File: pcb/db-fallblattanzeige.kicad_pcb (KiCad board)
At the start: 2 copper layers, 20 parts, among them IC1 ATMEGA328-P, IC2 MAX485, P1 2x9_pin_holes, P2 FTDI_header, Y1 Crystal

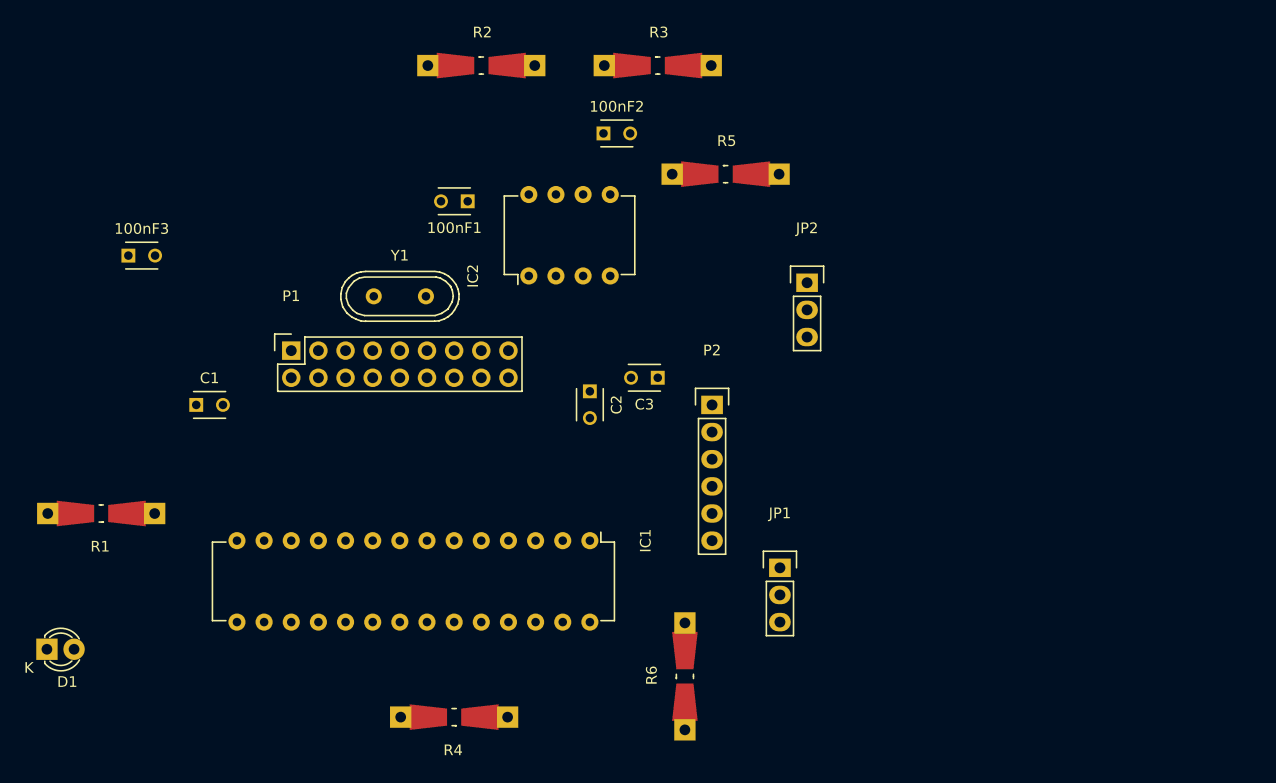
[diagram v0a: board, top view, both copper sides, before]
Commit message: improved pcb layout
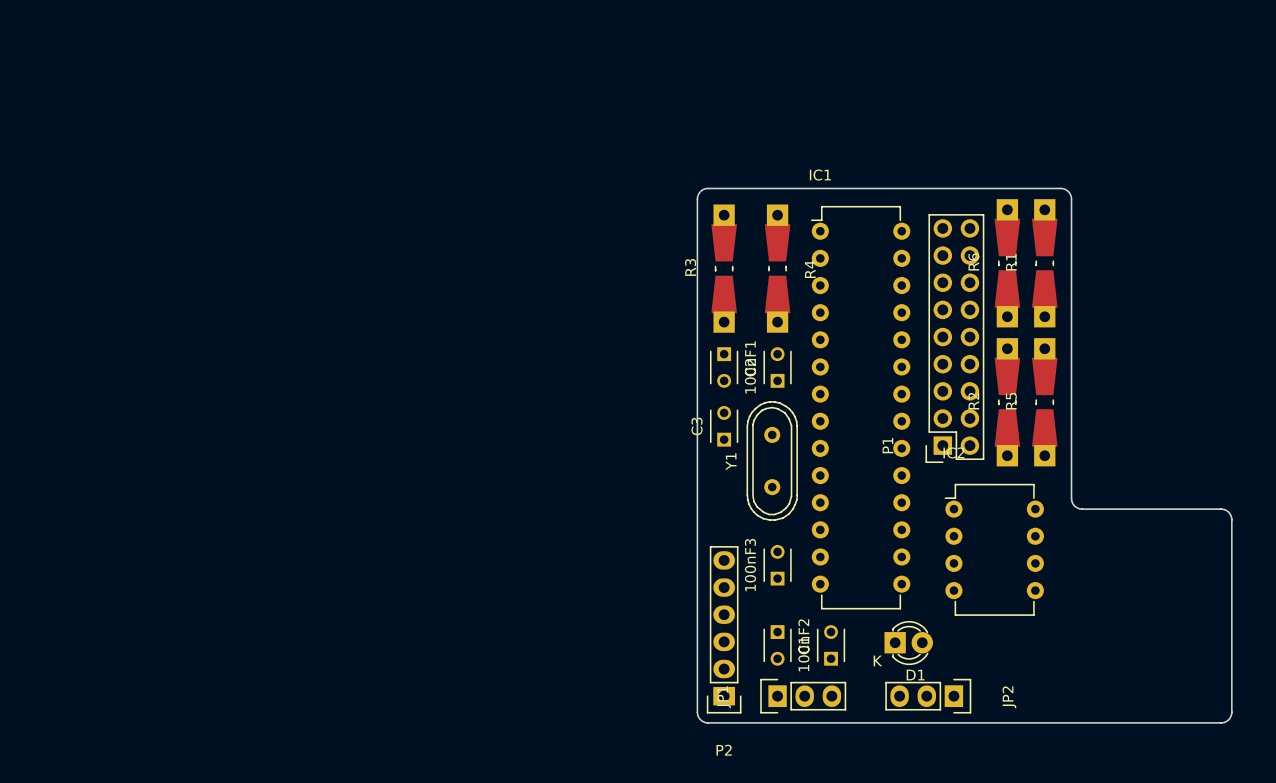
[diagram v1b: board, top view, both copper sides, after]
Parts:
- moved R1 91.3 mm to (197.5, 82.0), turned to 90 degrees
- moved D1 79.4 mm to (183.5, 117.5)
- moved 100nF3 67.8 mm to (172.5, 111.5), turned to 90 degrees
- moved P1 61.6 mm to (188.0, 99.1), turned to 90 degrees
- moved R2 58.4 mm to (194.0, 95.0), turned to 90 degrees
- moved C1 58.4 mm to (172.5, 116.5), turned to 270 degrees
- moved 100nF2 53.6 mm to (177.5, 119.0), turned to 90 degrees
- moved R4 51.7 mm to (172.5, 82.5), turned to 270 degrees
- moved R6 49.0 mm to (194.0, 82.0)
- moved IC2 45.4 mm to (189.0, 105.0), turned to 0 degrees
- moved JP2 41.0 mm to (189.0, 122.5), turned to 270 degrees
- moved Y1 38.1 mm to (172.0, 100.5), turned to 90 degrees
- moved R5 36.7 mm to (197.5, 95.0), turned to 90 degrees
- moved IC1 36.1 mm to (176.5, 79.0), turned to 0 degrees
- moved 100nF1 27.9 mm to (167.5, 90.5), turned to 270 degrees
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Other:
- board outline added: 50 x 50 mm

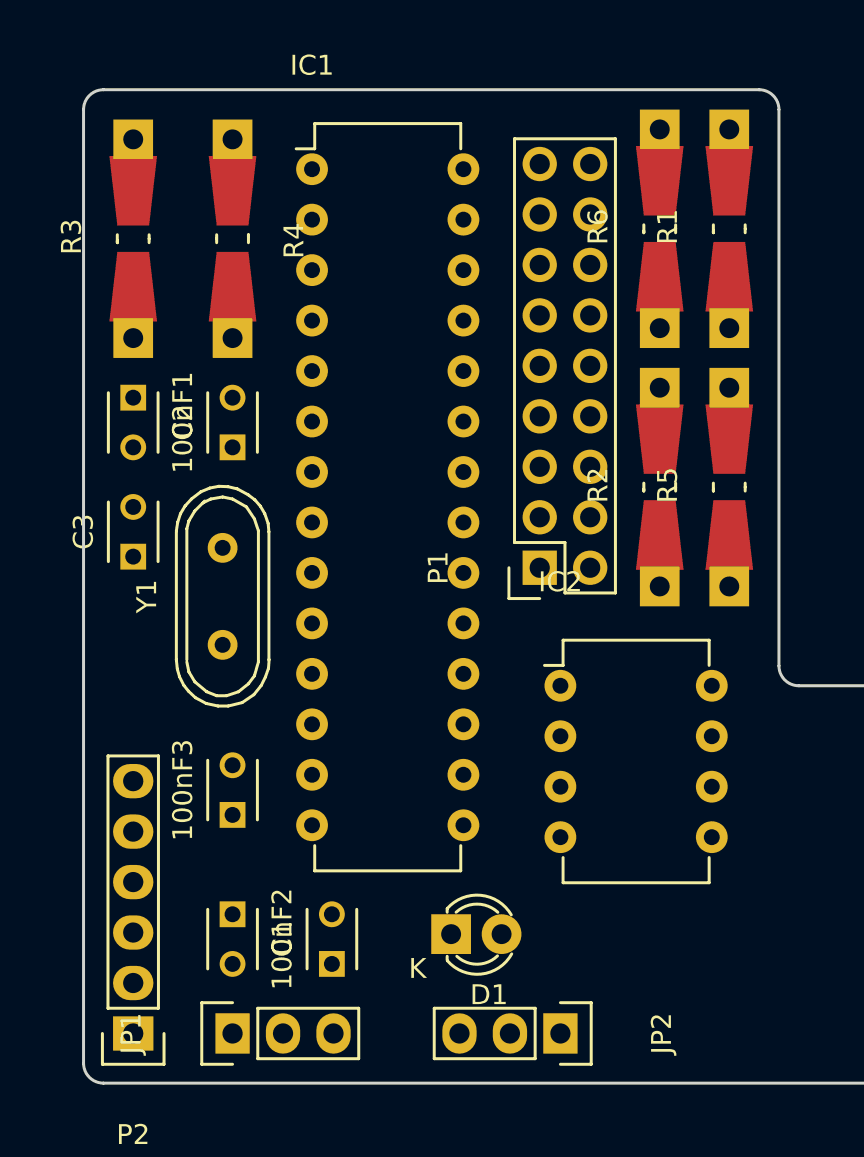
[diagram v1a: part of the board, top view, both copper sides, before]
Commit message: fix crystal wiring, blocking caps
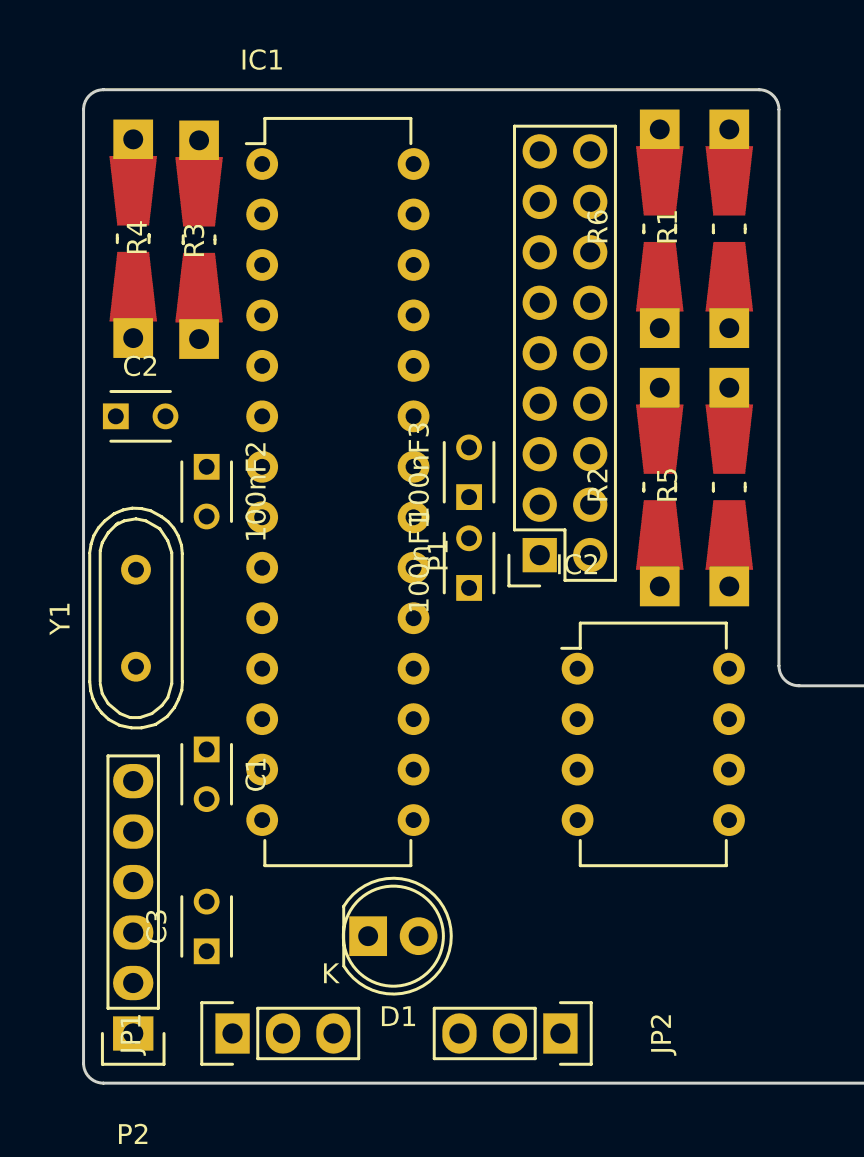
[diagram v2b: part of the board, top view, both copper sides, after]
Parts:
- D1: footprint LEDs:LED-3MM -> LEDs:LED-5MM
- moved 100nF2 25.8 mm to (171.2, 94.0), turned to 270 degrees
- moved C3 20.2 mm to (171.2, 118.4)
- moved 100nF3 19.9 mm to (184.4, 95.5)
- moved 100nF1 19.4 mm to (184.4, 100.1), turned to 90 degrees
- moved C1 8.40 mm to (171.2, 108.2)
- moved C2 6.08 mm to (166.6, 91.4), turned to 0 degrees
- moved Y1 4.50 mm to (167.6, 101.6)
- moved D1 4.18 mm to (179.3, 117.6)
- moved IC1 2.52 mm to (174.0, 78.7)
- moved R4 1.69 mm to (170.8, 82.5), turned to 90 degrees
- moved IC2 1.22 mm to (189.9, 104.1)
- moved P1 0.64 mm to (188.0, 98.4)
- turned R3 to 270 degrees
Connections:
- IC1 pad 10: Net-(IC1-Pad10) -> Net-(C2-Pad1)
- IC1 pad 16: Net-(IC1-Pad16) -> (no net)
- IC1 pad 17: Net-(IC1-Pad17) -> (no net)
- IC1 pad 18: Net-(IC1-Pad18) -> (no net)
- IC1 pad 19: Net-(IC1-Pad19) -> (no net)
- IC1 pad 23: Net-(IC1-Pad23) -> (no net)
- IC1 pad 24: Net-(IC1-Pad24) -> (no net)
- IC1 pad 6: Net-(IC1-Pad6) -> (no net)
- JP2 pad 1: Net-(JP2-Pad1) -> (no net)
- P1 pad 11: Net-(P1-Pad11) -> (no net)
- P1 pad 13: Net-(P1-Pad13) -> (no net)
- P1 pad 18: Net-(P1-Pad18) -> (no net)
- P1 pad 5: Net-(P1-Pad5) -> (no net)
- P1 pad 7: Net-(P1-Pad7) -> (no net)
- Y1 pad 1: Net-(IC1-Pad10) -> Net-(C1-Pad1)

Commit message: kicad: completed routing
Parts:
- moved C3 25.1 mm to (168.1, 93.4)
- moved D1 15.5 mm to (194.8, 118.4), turned to 180 degrees
- moved C2 8.45 mm to (166.5, 99.9), turned to 90 degrees
- moved C1 7.95 mm to (166.5, 101.8)
- moved 100nF2 3.05 mm to (171.3, 90.9)
- moved Y1 2.37 mm to (169.9, 101.0)
- moved JP1 1.55 mm to (174.1, 122.5)
- moved JP2 0.98 mm to (188.0, 122.5)
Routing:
- net VCC: track 0.00 -> 121.3 mm, vias 0 -> 4
- net GND: track 0.00 -> 100.0 mm, vias 0 -> 1
- net Net-(IC1-Pad3): track 0.00 -> 77.0 mm, vias 0 -> 2
- net Net-(IC1-Pad2): track 0.00 -> 74.2 mm, vias 0 -> 3
- net +5VD: track 0.00 -> 68.9 mm
- net Net-(D1-Pad2): track 0.00 -> 49.5 mm
- net Net-(IC1-Pad5): track 0.00 -> 46.9 mm, vias 0 -> 4
- net Net-(IC1-Pad4): track 0.00 -> 43.4 mm, vias 0 -> 2
- net /BUS_PLUS: track 0.00 -> 41.2 mm
- net /IR_IN: track 0.00 -> 34.4 mm, vias 0 -> 2
- net /BUS_MINUS: track 0.00 -> 30.7 mm
- net Net-(C3-Pad1): track 0.00 -> 30.2 mm
- net Net-(C3-Pad2): track 0.00 -> 29.4 mm
- net /SR_DATA: track 0.00 -> 28.2 mm, vias 0 -> 1
- net /SR_CP: track 0.00 -> 26.3 mm, vias 0 -> 1
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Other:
- net class Small Tracks added: clearance 0.2, trace_width 0.127, via_dia 0.6, via_drill 0.4
- rule trace_min: 0.2 -> 0.127

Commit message: add logo + FTDI header
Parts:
- added G***: LOGO, c-base-db:c-base-db, F.Cu at (207.5, 114.5)
- Debug Override: renamed from JP1
- Power Select: renamed from JP2
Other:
- board text added: "RTS RX TX VCC CTS GND"
- board text added: "coon@c-base.org 03/2016"

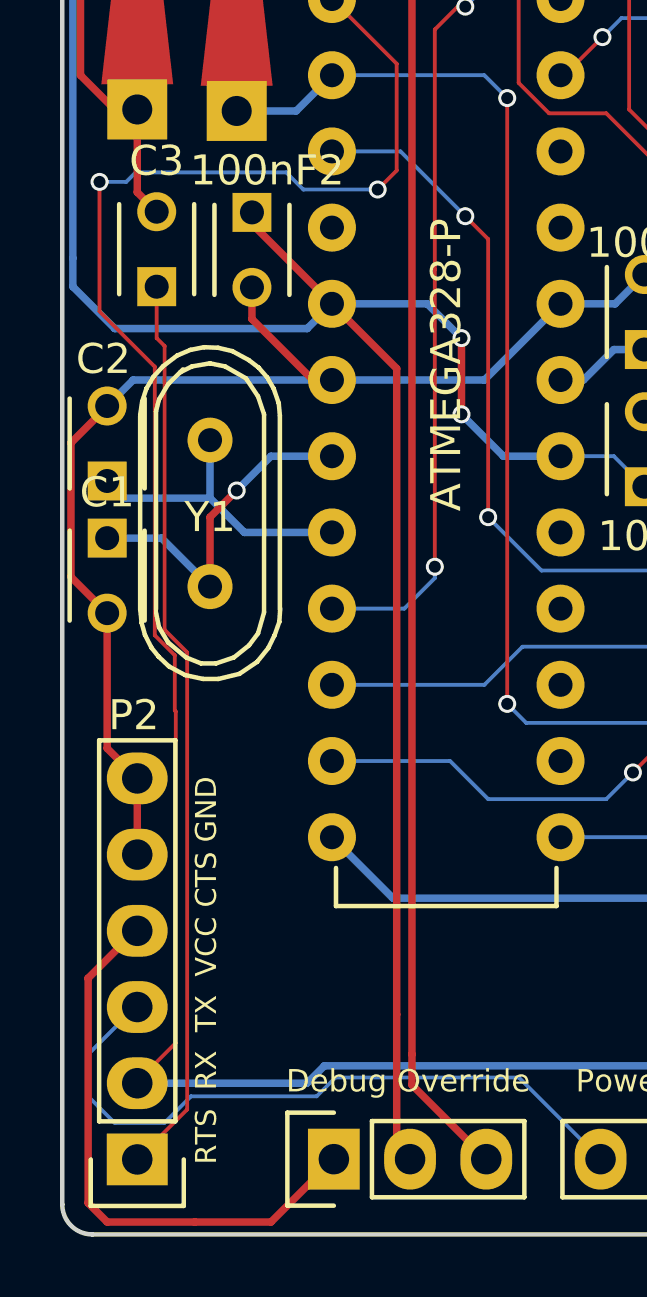
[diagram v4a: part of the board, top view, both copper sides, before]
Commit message: kicad: add some descriptions on silk
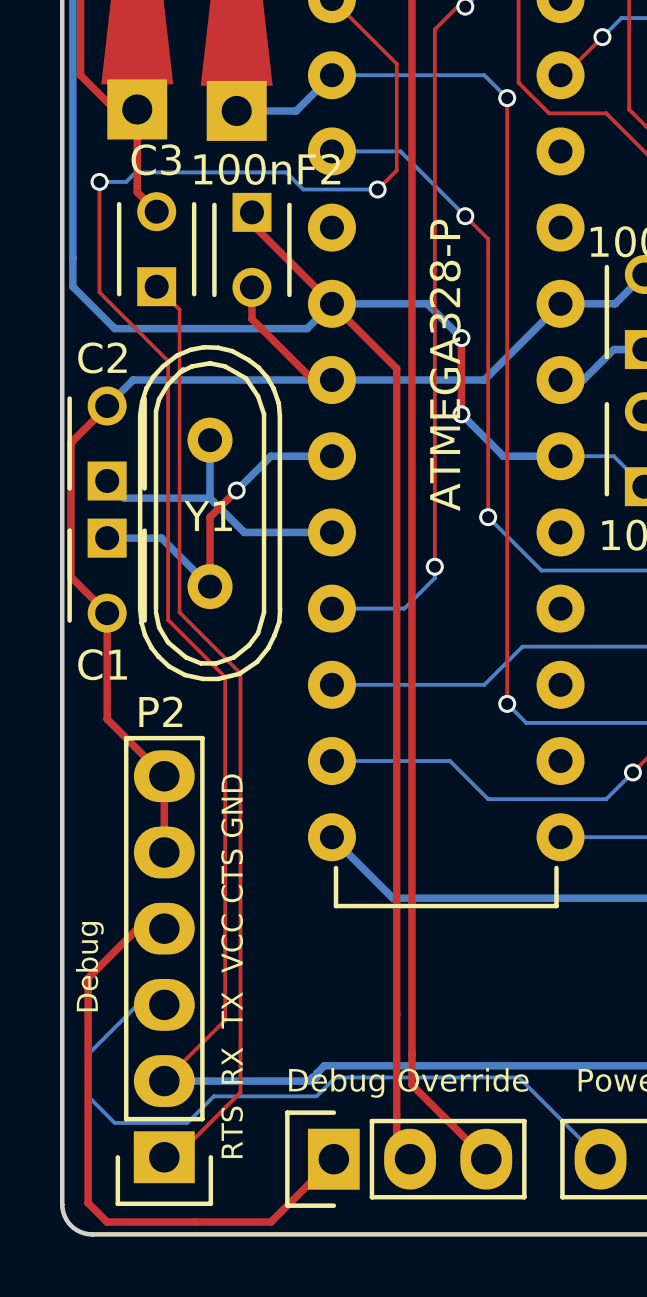
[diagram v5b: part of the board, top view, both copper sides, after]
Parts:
- moved P2 0.90 mm to (168.4, 122.4)
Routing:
- net Net-(C3-Pad1): track 30.2 -> 31.5 mm
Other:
- board text added: "Debug"

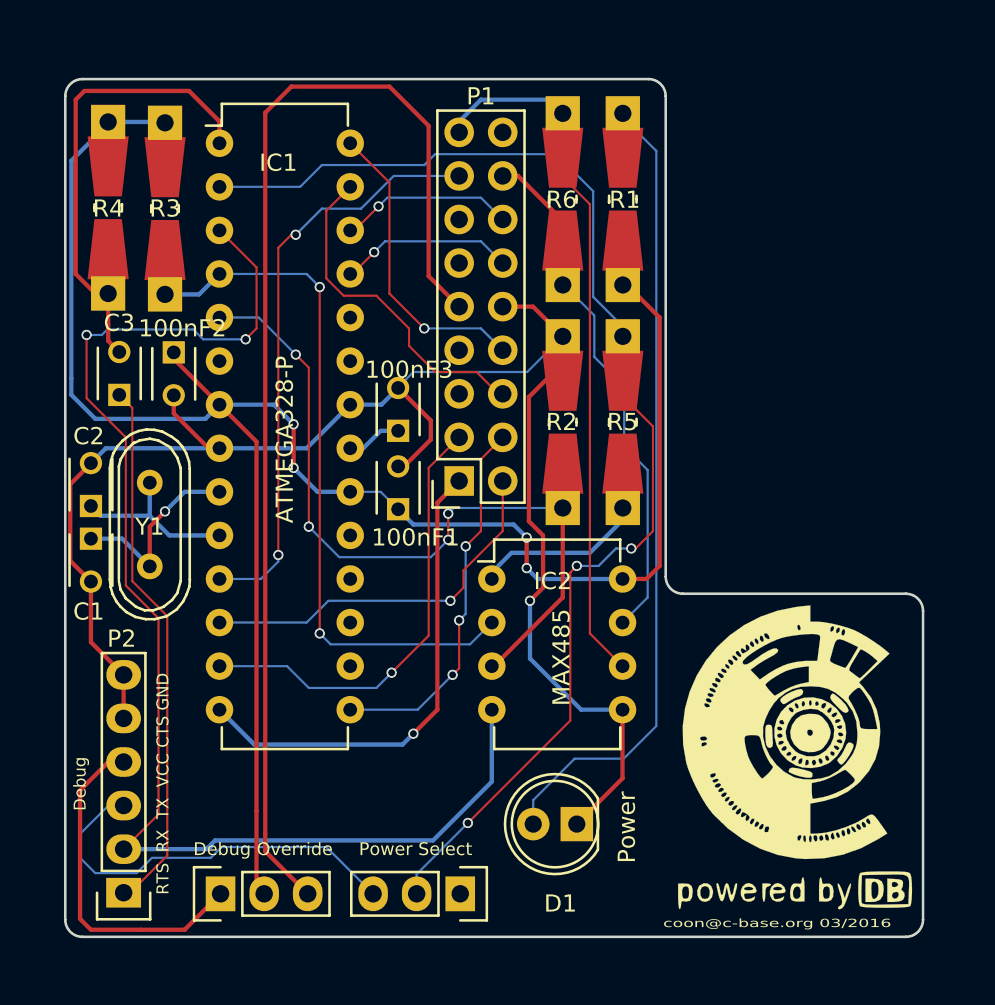
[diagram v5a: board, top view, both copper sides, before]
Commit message: kicad: add ground plane
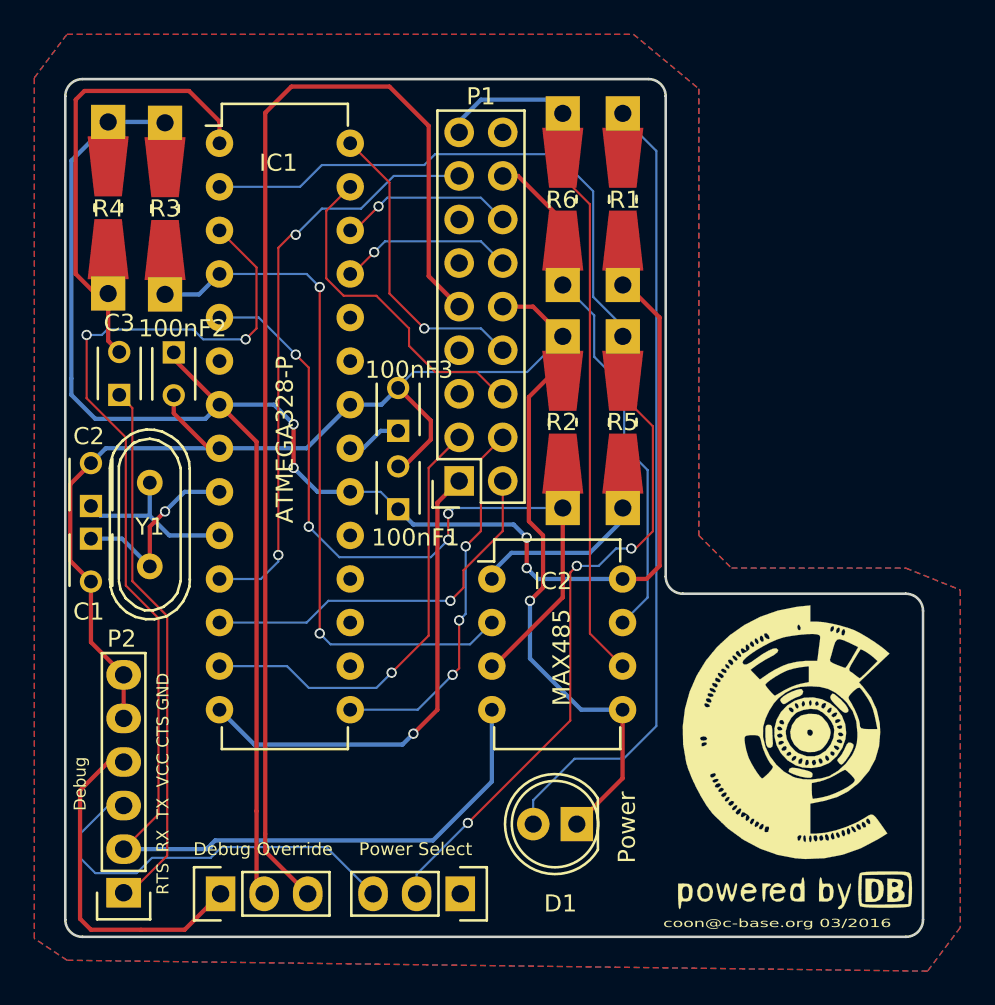
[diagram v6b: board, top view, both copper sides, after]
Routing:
- added copper zone on B.Cu, net GND
- added copper zone on F.Cu, net GND
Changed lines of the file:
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@@
     (user_trace_width 0.127)
     (trace_clearance 0.2)
-    (zone_clearance 0.508)
+    (zone_clearance 0.0108)
     (zone_45_only no)
     (trace_min 0.127)
@@
   (segment (start 170.815 80.137) (end 170.815 77.54874) (width 0.25) (layer F.Cu) (net 1))
   (segment (start 167.5 80.087) (end 167.5 77.49874) (width 0.25) (layer F.Cu) (net 1))
-  (segment (start 166.497 104.2905) (end 166.497 107.823) (width 0.25) (layer F.Cu) (net 2) (status 400000))
-  (segment (start 166.497 107.823) (end 168.402 109.728) (width 0.25) (layer F.Cu) (net 2) (status 800000))
-  (segment (start 168.402 109.728) (end 168.402 112.268) (width 0.25) (layer F.Cu) (net 2) (status C00000))
+  (segment (start 166.497 104.2905) (end 166.497 107.823) (width 0.25) (layer F.Cu) (net 2))
+  (segment (start 166.497 107.823) (end 168.402 109.728) (width 0.25) (layer F.Cu) (net 2))
+  (segment (start 168.402 109.728) (end 168.402 112.268) (width 0.25) (layer F.Cu) (net 2))
   (segment (start 197.485 111.76) (end 197.485 115.7605) (width 0.25) (layer F.Cu) (net 2))
   (segment (start 197.485 115.7605) (end 194.818 118.4275) (width 0.25) (layer F.Cu) (net 2))
@@
   (segment (start 173.482 120.396) (end 174.109498 119.768502) (width 0.127) (layer B.Cu) (net 27))
   (segment (start 174.109498 119.768502) (end 179.197 119.768502) (width 0.127) (layer B.Cu) (net 27))
+  (zone (net 2) (net_name GND) (layer F.Cu) (hatch edge 0.508)
+    (connect_pads (clearance 0.0108))
+    (min_thickness 0.054)
+    (fill yes (arc_segments 16) (thermal_gap 0.01) (thermal_bridge_width 0.16))
+    (polygon
+      (pts
+        (xy 165.1 72.39) (xy 198.12 72.39) (xy 201.93 75.565) (xy 201.93 101.6) (xy 203.835 103.505)
+        (xy 213.995 103.505) (xy 217.17 104.775) (xy 217.17 124.46) (xy 215.265 127) (xy 165.1 126.365)
+        (xy 163.195 125.095) (xy 163.195 74.93) (xy 165.1 72.39)
+      )
+    )
+  )
+  (zone (net 2) (net_name GND) (layer B.Cu) (hatch edge 0.508)
+    (connect_pads (clearance 0.0108))
+    (min_thickness 0.054)
+    (fill yes (arc_segments 16) (thermal_gap 0.01) (thermal_bridge_width 0.16))
+    (polygon
+      (pts
+        (xy 165.1 72.39) (xy 198.12 72.39) (xy 201.93 75.565) (xy 201.93 101.6) (xy 203.835 103.505)
+        (xy 213.995 103.505) (xy 217.17 104.775) (xy 217.17 124.46) (xy 215.265 127) (xy 165.1 126.365)
+        (xy 163.195 125.095) (xy 163.195 74.93) (xy 165.1 72.39)
+      )
+    )
+  )
 )
